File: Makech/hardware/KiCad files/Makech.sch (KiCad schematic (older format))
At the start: 46 parts, among them IC1 ULN2803, J1 SWD programmer, J2 USB_B_Micro, J3 ESP32-Exp, SW1 RST, SW2 SW_DPDT_x2, U1 ATSAMD21G18A-AU, U2 CONN_01X04, U3 AP2114_3.3v, X1 Screw_Terminal_1x02

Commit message: FOOTPRINT
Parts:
- J1: footprint Pines:621X0421021 -> Connector_PinHeader_2.54mm:PinHeader_2x02_P2.54mm_Vertical_SMD
- JP1: footprint (none) -> Jumper:SolderJumper-2_P1.3mm_Bridged_RoundedPad1.0x1.5mm
- LED1, LED2, LED3, LED4: footprint LEDs:LED_D3.0mm -> LED_THT:LED_D3.0mm
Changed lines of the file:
@@
 F 0 "LED1" H 5755 3060 40  0000 C CNN
 F 1 "L" H 5755 2860 40  0001 C CNN
-F 2 "LEDs:LED_D3.0mm" H 5755 2960 60  0001 C CNN
+F 2 "LED_THT:LED_D3.0mm" H 5755 2960 60  0001 C CNN
 F 3 "" H 5755 2960 60  0000 C CNN
 F 4 "APT2012LVBC/D" H 5755 2960 50  0001 C CNN "manf#"
@@
 F 0 "LED2" H 6385 3060 40  0000 C CNN
 F 1 "L" H 6385 2860 40  0001 C CNN
-F 2 "LEDs:LED_D3.0mm" H 6385 2960 60  0001 C CNN
+F 2 "LED_THT:LED_D3.0mm" H 6385 2960 60  0001 C CNN
 F 3 "" H 6385 2960 60  0000 C CNN
 F 4 "APT2012SRCPRV" H 6385 2960 50  0001 C CNN "manf#"
@@
 F 0 "LED3" H 7015 3060 40  0000 C CNN
 F 1 "L" H 7015 2860 40  0001 C CNN
-F 2 "LEDs:LED_D3.0mm" H 7015 2960 60  0001 C CNN
+F 2 "LED_THT:LED_D3.0mm" H 7015 2960 60  0001 C CNN
 F 3 "" H 7015 2960 60  0000 C CNN
 F 4 "APT2012SECK" H 7015 2960 50  0001 C CNN "manf#"
@@
 F 0 "LED4" H 7645 3060 40  0000 C CNN
 F 1 "L" H 7645 2860 40  0001 C CNN
-F 2 "LEDs:LED_D3.0mm" H 7645 2960 60  0001 C CNN
+F 2 "LED_THT:LED_D3.0mm" H 7645 2960 60  0001 C CNN
 F 3 "" H 7645 2960 60  0000 C CNN
 F 4 "APT2012SGC" H 7645 2960 50  0001 C CNN "manf#"
@@
 F 0 "J1" H 1305 5897 50  0000 C CNN
 F 1 "SWD programmer" H 1305 5806 50  0000 C CNN
-F 2 "Pines:621X0421021" H 1255 5680 50  0001 C CNN
+F 2 "Connector_PinHeader_2.54mm:PinHeader_2x02_P2.54mm_Vertical_SMD" H 1255 5680 50  0001 C CNN
 F 3 "~" H 1255 5680 50  0001 C CNN
 	1    1255 5680
@@
 F 0 "JP1" V 4054 5533 50  0000 L CNN
 F 1 "Jumper" H 3980 5380 50  0000 L CNN
-F 2 "" H 4100 5465 50  0001 C CNN
+F 2 "Jumper:SolderJumper-2_P1.3mm_Bridged_RoundedPad1.0x1.5mm" H 4100 5465 50  0001 C CNN
 F 3 "~" H 4100 5465 50  0001 C CNN
 	1    4100 5465

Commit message: PCB
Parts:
- removed R7, R8: 10K, Resistor_SMD:R_0805_2012Metric_Pad1.15x1.40mm_HandSolder, symbol Device:R_Small
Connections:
- net ESP_CS is gone; now on net +3V3: J3.3 (Pin_3), U1.23 (PA14)
- net ESP_RESET is gone; now on net GND: J3.11 (Pin_11), U1.32 (PA23)
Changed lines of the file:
@@
 Wire Wire Line
 	2940 1305 2940 1405
-$Comp
-L Device:R_Small R7
-U 1 1 5C89865A
-P 6630 4980
-F 0 "R7" H 6689 5026 50  0000 L CNN
-F 1 "10K" H 6689 4935 50  0000 L CNN
-F 2 "Resistor_SMD:R_0805_2012Metric_Pad1.15x1.40mm_HandSolder" H 6630 4980 50  0001 C CNN
-F 3 "~" H 6630 4980 50  0001 C CNN
-F 4 "CRCW080510K0FKEAC" H 6630 4980 50  0001 C CNN "manf#"
-	1    6630 4980
-	-1   0    0    1
-$EndComp
-Wire Wire Line
-	6630 5450 6630 5080
 Wire Wire Line
 	6630 5450 6880 5450
-Wire Wire Line
-	6630 4880 6630 4820
 $Comp
 L power:+3.3V #PWR022
 U 1 1 5C8EBAE6
-P 6630 4820
-F 0 "#PWR022" H 6630 4670 50  0001 C CNN
-F 1 "+3.3V" H 6645 4993 50  0000 C CNN
-F 2 "" H 6630 4820 50  0001 C CNN
-F 3 "" H 6630 4820 50  0001 C CNN
-	1    6630 4820
+P 6630 5025
+F 0 "#PWR022" H 6630 4875 50  0001 C CNN
+F 1 "+3.3V" H 6645 5198 50  0000 C CNN
+F 2 "" H 6630 5025 50  0001 C CNN
+F 3 "" H 6630 5025 50  0001 C CNN
+	1    6630 5025
 	1    0    0    -1
 $EndComp
 Wire Wire Line
-	8165 5650 8165 5780
-Wire Wire Line
 	7380 5650 8165 5650
-$Comp
-L Device:R_Small R8
-U 1 1 5C967BAB
-P 8165 5880
-F 0 "R8" H 8224 5926 50  0000 L CNN
-F 1 "10K" H 8224 5835 50  0000 L CNN
-F 2 "Resistor_SMD:R_0805_2012Metric_Pad1.15x1.40mm_HandSolder" H 8165 5880 50  0001 C CNN
-F 3 "~" H 8165 5880 50  0001 C CNN
-F 4 "CRCW080510K0FKEAC" H 8165 5880 50  0001 C CNN "manf#"
-	1    8165 5880
-	1    0    0    -1
-$EndComp
-Wire Wire Line
-	8165 5980 8165 6015
-$Comp
-L power:GND #PWR025
-U 1 1 5C99179E
-P 8165 6015
-F 0 "#PWR025" H 8165 5765 50  0001 C CNN
-F 1 "GND" H 8170 5842 50  0000 C CNN
-F 2 "" H 8165 6015 50  0001 C CNN
-F 3 "" H 8165 6015 50  0001 C CNN
-	1    8165 6015
-	1    0    0    -1
-$EndComp
 Text Label 1245 3905 2    60   ~ 0
 ESP_RESET
@@
 Text Notes 2570 6715 0    118  ~ 0
 SOURCE
+$Comp
+L power:GND #PWR025
+U 1 1 5C99179E
+P 8165 5780
+F 0 "#PWR025" H 8165 5530 50  0001 C CNN
+F 1 "GND" H 8170 5607 50  0000 C CNN
+F 2 "" H 8165 5780 50  0001 C CNN
+F 3 "" H 8165 5780 50  0001 C CNN
+	1    8165 5780
+	1    0    0    -1
+$EndComp
+Wire Wire Line
+	8165 5650 8165 5780
+Wire Wire Line
+	6630 5025 6630 5450
 $EndSCHEMATC

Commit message: foot-print change
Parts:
- XH1, XH2: footprint Connector_Molex:Molex_KK-254_AE-6410-05A_1x05_P2.54mm_Vertical -> ElectronicCats-KiCad-Libraries:Molex_KK-254_AE-6410-05A_1x05_P2.54mm_Vertical
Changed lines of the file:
@@
 F 0 "XH2" H 11045 6005 50  0000 C CNN
 F 1 "CONN_01X05" V 11145 5705 50  0001 C CNN
-F 2 "Connector_Molex:Molex_KK-254_AE-6410-05A_1x05_P2.54mm_Vertical" H 11045 5705 50  0001 C CNN
+F 2 "ElectronicCats-KiCad-Libraries:Molex_KK-254_AE-6410-05A_1x05_P2.54mm_Vertical" H 11045 5705 50  0001 C CNN
 F 3 "" H 11045 5705 50  0000 C CNN
 F 4 "B5B-XH-A (LF)(SN) " H 11045 5705 50  0001 C CNN "manf#"
@@
 F 0 "XH1" H 11045 4520 50  0000 C CNN
 F 1 "CONN_01X05" V 11145 4810 50  0001 C CNN
-F 2 "Connector_Molex:Molex_KK-254_AE-6410-05A_1x05_P2.54mm_Vertical" H 11045 4810 50  0001 C CNN
+F 2 "ElectronicCats-KiCad-Libraries:Molex_KK-254_AE-6410-05A_1x05_P2.54mm_Vertical" H 11045 4810 50  0001 C CNN
 F 3 "" H 11045 4810 50  0000 C CNN
 F 4 "B5B-XH-A (LF)(SN) " H 11045 4810 50  0001 C CNN "manf#"

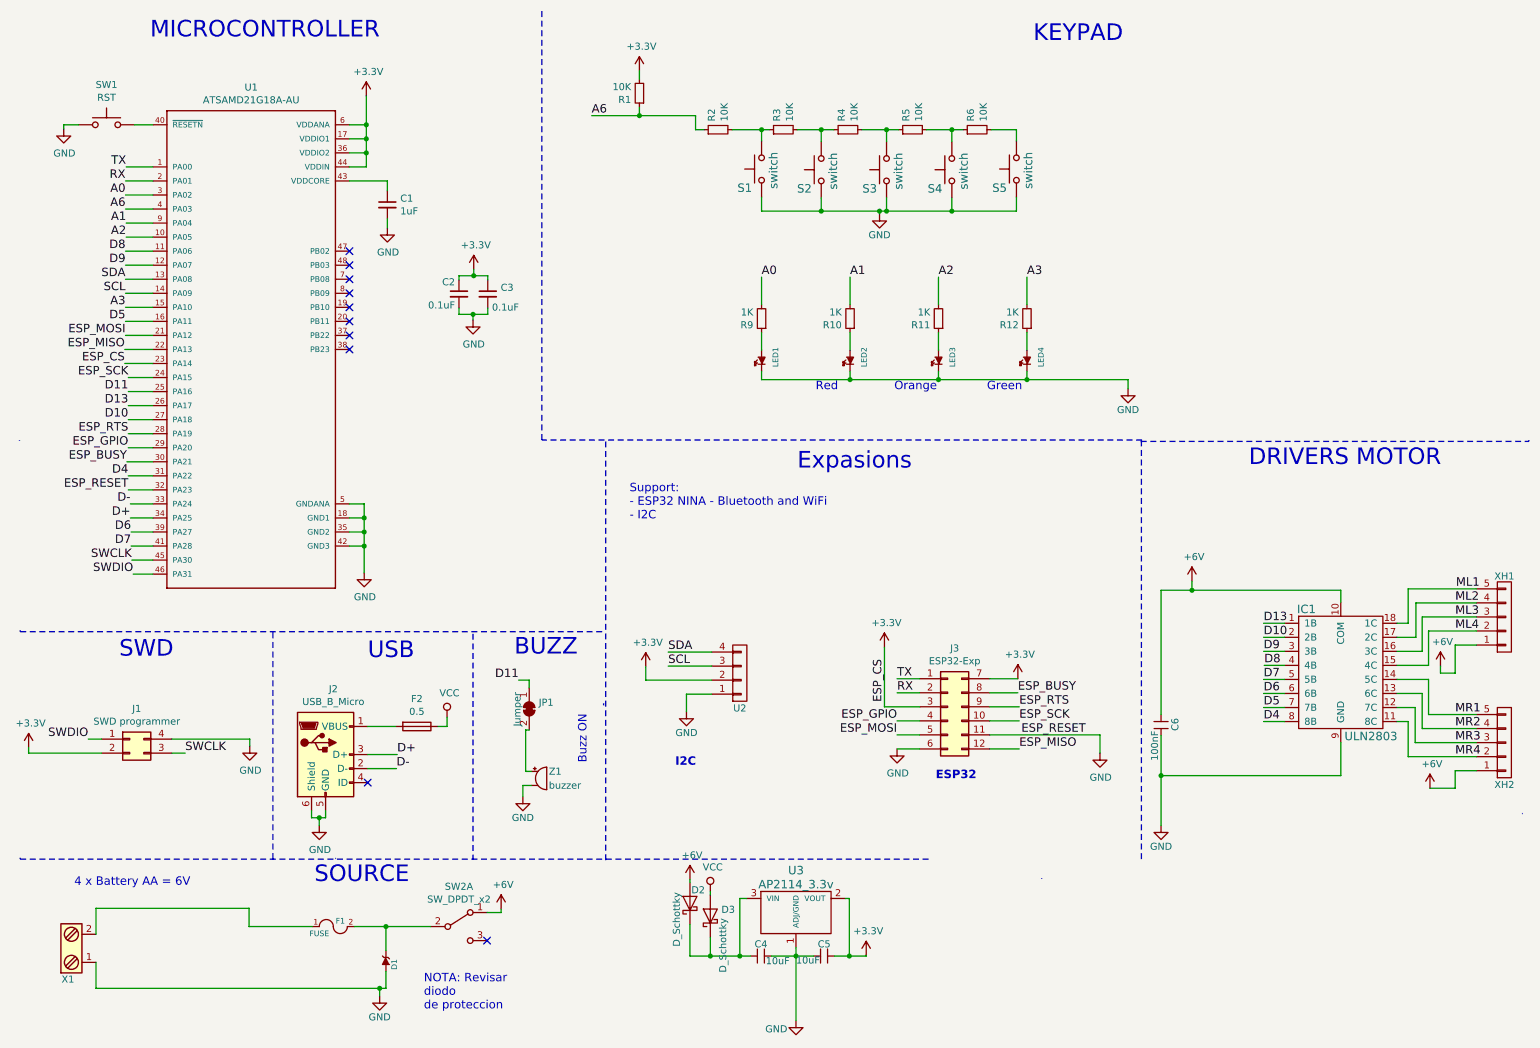
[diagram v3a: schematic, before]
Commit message: Re-define pins for Arduino and Makecode in Schematic
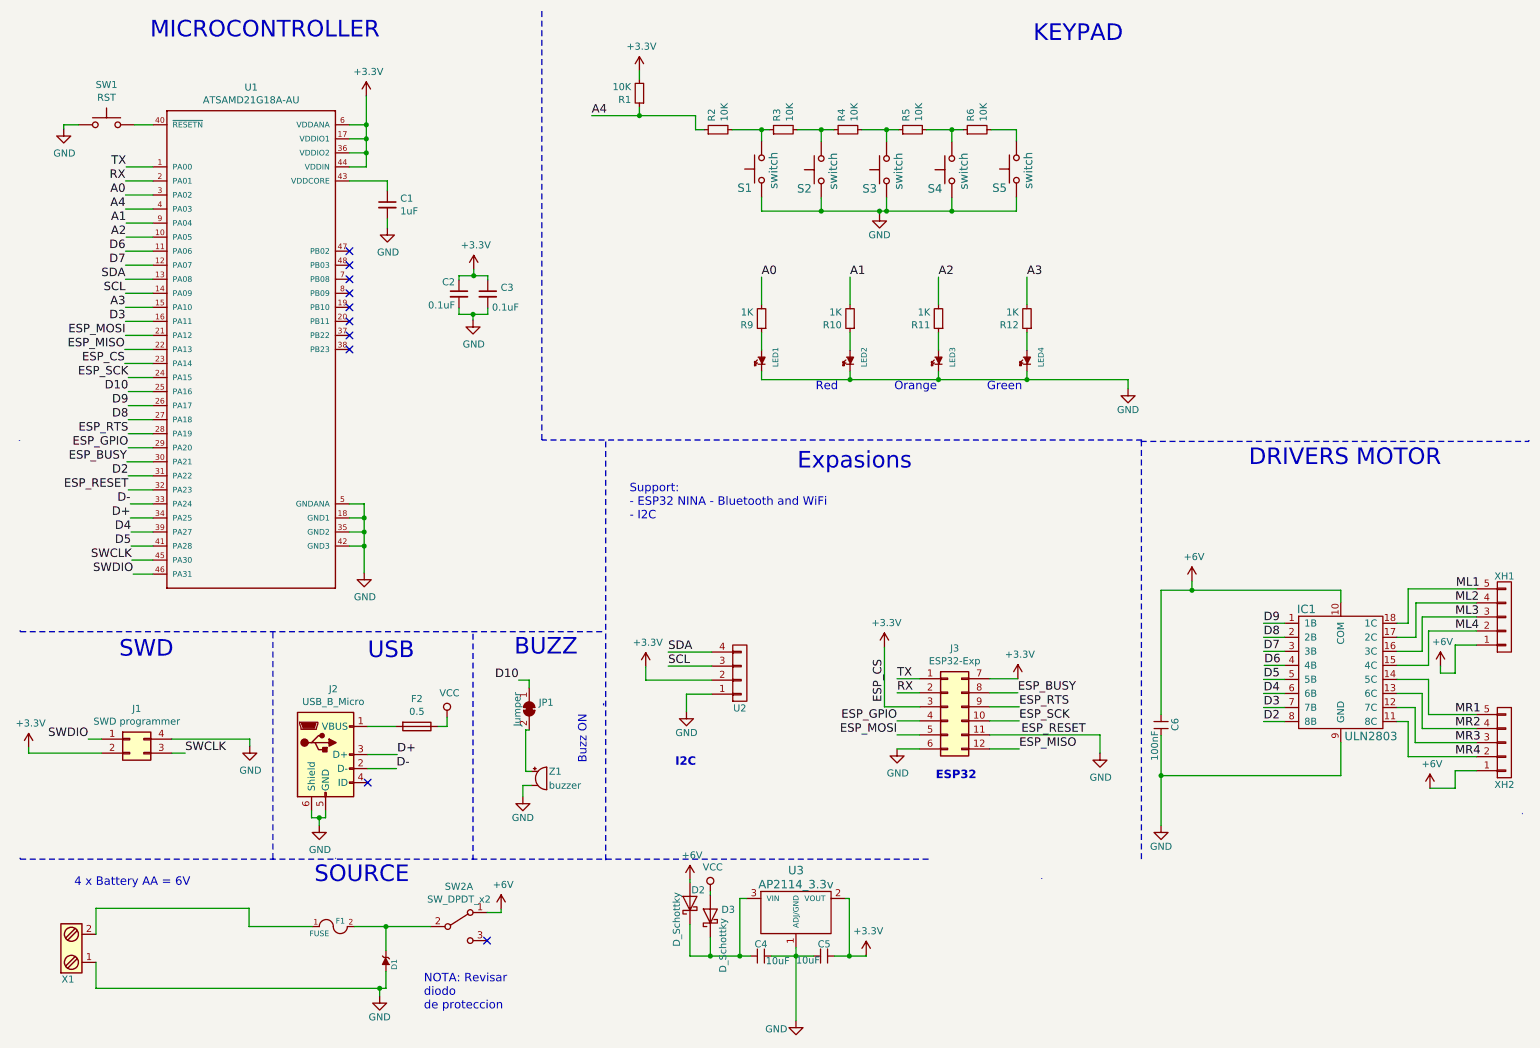
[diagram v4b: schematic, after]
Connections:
- net D11 is gone; now on net D10: JP1.1 (A), U1.25 (PA16)
- net D13 is gone; now on net D9: IC1.1 (1B), U1.26 (PA17)
- net D10: no longer IC1.2 (2B), U1.27 (PA18)
- net D4: now also IC1.6 (6B), U1.39 (PA27); no longer IC1.8 (8B), U1.31 (PA22)
- net D5: now also IC1.5 (5B), U1.41 (PA28); no longer IC1.7 (7B), U1.16 (PA11)
- net D6: now also IC1.4 (4B), U1.11 (PA06); no longer IC1.6 (6B), U1.39 (PA27)
- net D7: now also IC1.3 (3B), U1.12 (PA07); no longer IC1.5 (5B), U1.41 (PA28)
- net D8: now also IC1.2 (2B), U1.27 (PA18); no longer IC1.4 (4B), U1.11 (PA06)
- net D9: no longer IC1.3 (3B), U1.12 (PA07)
- net A6 renamed A4
- new net D2: IC1.8 (8B), U1.31 (PA22)
- new net D3: IC1.7 (7B), U1.16 (PA11)
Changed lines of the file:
@@
 Sheet 1 1
 Title "Escornabot Makech"
-Date "2019-03-03"
-Rev "v0.2"
+Date "2019-04-28"
+Rev "v0.3"
 Comp "Electronic Cats"
 Comment1 "Andres Sabas"
@@
 $EndComp
 Text Label 4025 5260 2    60   ~ 0
-D11
+D10
 $Comp
 L Makech-rescue:GND--Ogaki-rescue-Makech-rescue-Makech-rescue-Makech-rescue-Makech-rescue-Makech-rescue-Makech-rescue-Makech-rescue-Makech-rescue #PWR013
@@
 $EndComp
 Text Label 9330 4855 0    60   ~ 0
-D13
+D9
 Text Label 9330 4955 0    60   ~ 0
-D10
+D8
 Text Label 9330 5055 0    60   ~ 0
-D9
+D7
 Text Label 9335 5155 0    60   ~ 0
-D8
+D6
 Text Label 9330 5255 0    60   ~ 0
-D7
+D5
 Text Label 9330 5355 0    60   ~ 0
-D6
+D4
 Text Label 9330 5455 0    60   ~ 0
-D5
+D3
 Text Label 9330 5555 0    60   ~ 0
-D4
+D2
 Text Label 10700 4610 0    60   ~ 0
 ML1
@@
 SCL
 Text Label 1245 3805 2    60   ~ 0
+D2
+Text Label 1225 2705 2    60   ~ 0
+D3
+Text Label 1265 4205 2    60   ~ 0
 D4
-Text Label 1225 2705 2    60   ~ 0
+Text Label 1265 4305 2    60   ~ 0
 D5
-Text Label 1265 4205 2    60   ~ 0
+Text Label 1225 2205 2    60   ~ 0
 D6
-Text Label 1265 4305 2    60   ~ 0
+Text Label 1225 2305 2    60   ~ 0
 D7
-Text Label 1225 2205 2    60   ~ 0
+Text Label 1245 3405 2    60   ~ 0
 D8
-Text Label 1225 2305 2    60   ~ 0
+Text Label 1245 3305 2    60   ~ 0
 D9
-Text Label 1245 3405 2    60   ~ 0
+Text Label 1245 3205 2    60   ~ 0
 D10
-Text Label 1245 3305 2    60   ~ 0
-D13
-Text Label 1245 3205 2    60   ~ 0
-D11
 Text Notes 1400 700  0    118  ~ 0
 MICROCONTROLLER
@@
 ESP_RESET
 Text Label 4545 1240 0    60   ~ 0
-A6
+A4
 Text Label 1225 1905 2    60   ~ 0
-A6
+A4
 Text Label 1245 3605 2    60   ~ 0
 ESP_GPIO

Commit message: Change connector ESP32, SWD and logo OSWHA
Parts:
- J1: footprint Connector_PinHeader_2.54mm:PinHeader_2x02_P2.54mm_Vertical_SMD -> Pines:621X04245821
- J3: footprint Connector_PinHeader_1.00mm:PinHeader_2x06_P1.00mm_Vertical_SMD -> Pines:610X1221121
- Z1: footprint Buzzer_Beeper:MagneticBuzzer_StarMicronics_HMB-06_HMB-12 -> Buzzers_Beepers:MagneticBuzzer_ProSignal_ABI-009-RC
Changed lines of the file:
@@
 F 0 "Z1" H 4240 6010 50  0000 L CNN
 F 1 "buzzer" H 4240 5910 50  0000 L CNN
-F 2 "Buzzer_Beeper:MagneticBuzzer_StarMicronics_HMB-06_HMB-12" H 4165 5960 60  0001 C CNN
+F 2 "Buzzers_Beepers:MagneticBuzzer_ProSignal_ABI-009-RC" H 4165 5960 60  0001 C CNN
 F 3 "" H 4165 5960 60  0000 C CNN
 F 4 "F/CM12P-LF" H 4165 5960 50  0001 C CNN "manf#"
@@
 F 0 "J1" H 1305 5897 50  0000 C CNN
 F 1 "SWD programmer" H 1305 5806 50  0000 C CNN
-F 2 "Connector_PinHeader_2.54mm:PinHeader_2x02_P2.54mm_Vertical_SMD" H 1255 5680 50  0001 C CNN
+F 2 "Pines:621X04245821" H 1255 5680 50  0001 C CNN
 F 3 "~" H 1255 5680 50  0001 C CNN
 	1    1255 5680
@@
 F 0 "J3" H 7130 5867 50  0000 C CNN
 F 1 "ESP32-Exp" H 7130 5776 50  0000 C CNN
-F 2 "Connector_PinHeader_1.00mm:PinHeader_2x06_P1.00mm_Vertical_SMD" H 7080 5450 50  0001 C CNN
+F 2 "Pines:610X1221121" H 7080 5450 50  0001 C CNN
 F 3 "~" H 7080 5450 50  0001 C CNN
 F 4 "ESP32" H 7080 5450 50  0001 C CNN "manf#"

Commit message: change terminal block
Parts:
- X1: footprint TerminalBlock:TerminalBlock_Altech_AK300-2_P5.00mm -> Terminal_Blocks:TerminalBlock_bornier-2_P5.08mm
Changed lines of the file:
@@
 F 0 "X1" H 815 7420 50  0000 C TNN
 F 1 "Screw_Terminal_1x02" V 665 7170 50  0001 C TNN
-F 2 "TerminalBlock:TerminalBlock_Altech_AK300-2_P5.00mm" H 815 6945 50  0001 C CNN
+F 2 "Terminal_Blocks:TerminalBlock_bornier-2_P5.08mm" H 815 6945 50  0001 C CNN
 F 3 "" H 790 7170 50  0001 C CNN
 	1    815  7170
